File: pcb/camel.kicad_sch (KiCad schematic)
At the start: 49 parts, among them J1 Conn_01x04, J2 Conn_01x04, Q1 MMBT4403, Q2 MMBT4403, U1 HX711, U2 HX711, U3 MCP1700T-3302E/TT, Y1 11.0592MHz, Y2 11.0592MHz

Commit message: first pass
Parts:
- removed C13: 10u, Capacitor_SMD:C_0603_1608Metric, symbol Device:C_Small
- removed FPC1: FPC-05F-12PH15, EasyEDA2KiCAD:FPC-SMD_12P-P0.50_XUNPU_FPC-05F-12PH15, symbol EasyEDA2KiCAD:FPC-05F-12PH15
- removed JP1, JP4, JP6: SolderJumper_2_Bridged, Jumper:SolderJumper-2_P1.3mm_Bridged_RoundedPad1.0x1.5mm, symbol Jumper:SolderJumper_2_Bridged
- removed JP2, JP3: SolderJumper_3_Bridged12, Jumper:SolderJumper-3_P1.3mm_Bridged12_RoundedPad1.0x1.5mm, symbol Jumper:SolderJumper_3_Bridged12
- removed JP5, JP7: SolderJumper_2_Open, Jumper:SolderJumper-2_P1.3mm_Open_RoundedPad1.0x1.5mm, symbol Jumper:SolderJumper_2_Open
- removed R10, R9: 20K, Resistor_SMD:R_0402_1005Metric, symbol Device:R_Small
- removed Y1, Y2: 11.0592MHz, Crystal:Crystal_SMD_5032-4Pin_5.0x3.2mm, symbol Device:Crystal_GND24_Small
- added C15, C7, C8: 100n, Capacitor_SMD:C_0402_1005Metric, symbol Device:C_Small
- added C3: 10n, Capacitor_SMD:C_0402_1005Metric, symbol Device:C_Small
- added C4: 1u, Capacitor_SMD:C_0402_1005Metric, symbol Device:C_Small
- added D1: RED, LED_SMD:LED_0603_1608Metric, symbol Device:LED_Small
- added D10, D11, D2, D3, D4, D5, D6, D7, D8, D9: RCLAMP0521P-N, camel:X1-DFN1006-2_L1.0-W0.6-BI, symbol camel:RCLAMP0521P-N
- added H3, H4: MountingHole, MountingHole:MountingHole_3.5mm, symbol Mechanical:MountingHole
- added J2: TC2030-NL, Connector:Tag-Connect_TC2030-IDC-NL_2x03_P1.27mm_Vertical, symbol Connector:Conn_ARM_SWD_TagConnect_TC2030-NL
- added J3: USART, Connector_JST:JST_PH_S4B-PH-K_1x04_P2.00mm_Horizontal, symbol Connector_Generic:Conn_01x04
- added J5: I2C STEMMA, Connector_JST:JST_PH_S4B-PH-K_1x04_P2.00mm_Horizontal, symbol Connector_Generic:Conn_01x04
- added L1: 39n, Inductor_SMD:L_1008_2520Metric, symbol Device:L_Small
- added R4: 2K2, Resistor_SMD:R_0402_1005Metric, symbol Device:R_Small
- added R8: 10K, Resistor_SMD:R_0402_1005Metric, symbol Device:R_Small
- added U3: STM32L010F4P6, Package_SO:TSSOP-20_4.4x6.5mm_P0.65mm, symbol MCU_ST_STM32L0:STM32L010F4Px
- C10: value 10u -> 100n; footprint Capacitor_SMD:C_0603_1608Metric -> Capacitor_SMD:C_0402_1005Metric; Comment 25V 10uF X5R ±20% 0603 Multilayer Ceramic Capacitors MLCC -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 -> 16V 100nF X7R ±10% 0402 Multilayer Ceramic Capacitors MLCC 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; LCSC C96446 -> C1525; MFRN CL10A106MA8NRNC -> CL05B104KO5NNNC; PKG 0603 -> 0402
- C9: renamed from C14; value 0.1u -> 100n
- J1: footprint dualScaleBoard_hx711:Pad_1x04_P2.54mm -> camel:Pad_1x04_P2.54mm
- J4: renamed from J2; footprint dualScaleBoard_hx711:Pad_1x04_P2.54mm -> camel:Pad_1x04_P2.54mm
- Q1, Q2: symbol PCM_Transistor_BJT_AKL:MMBT4403 -> Transistor_BJT:MMBT3906
- U2: renamed from U1; footprint EasyEDA2KiCAD:SOP-16_L10.0-W3.9-P1.27-LS6.0-BL -> Package_SO:SOP-16_3.9x9.9mm_P1.27mm
- U4: renamed from U2; footprint EasyEDA2KiCAD:SOP-16_L10.0-W3.9-P1.27-LS6.0-BL -> Package_SO:SOP-16_3.9x9.9mm_P1.27mm
- renumbered C15 to C1, C1 to C11, C3 to C12, C5 to C13, C7 to C14, C2 to C17, C4 to C18, C6 to C19, C9 to C2, C8 to C20, C11 to C5, C12 to C6, H101 to H1, H102 to H2, L1 to L2, L2 to L3, R5 to R1, R8 to R10, R3 to R11, R4 to R12, R6 to R2, R1 to R3, R2 to R5, R7 to R9, U3 to U1
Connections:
- net VO is gone; now on net +3V3: U1.2 (VO)
- net DOUT1: now also U3.13 (PA7)
- net DOUT2: now also U3.12 (PA6)
- net GND: now also U2.14 (XI), U2.15 (RATE), U4.14 (XI), U4.15 (RATE), C15.1, C3.2, C4.2, C7.2, C8.2, D1.1 (K), D10.1, D11.1, D2.2, D3.2, D4.2, D5.2, D6.2, D7.2, D8.2, D9.2, J2.5 (GND), J3.4 (Pin_4), J5.4 (Pin_4), R8.2, U3.15 (VSS)
- net SCK1: now also U3.14 (PB1)
- net SCK2: now also U3.11 (PA5)
- net VCC renamed +5VA
- net +5VA: now also C3.1, C4.1, L1.1; no longer C10.1, C5.1, U1.3 (VI)
- net VDD renamed +3V3
- net +3V3: now also C10.1, C7.1, C8.1, D2.1, D6.1, J2.1 (VCC), J3.1 (Pin_1), U3.16 (VDD), U3.5 (VDDA)
- new net: D1.2 (A), R4.2
- new net +5V: C5.1, D9.1, J5.3 (Pin_3), L1.2, U1.3 (VI)
- new net BOOT0: R8.1, U3.1 (PB9)
- new net I2C_SCL: D10.2, J5.1 (Pin_1), U3.17 (PA9)
- new net I2C_SDA: D11.2, J5.2 (Pin_2), U3.18 (PA10)
- new net LED1: R4.1, U3.2 (PC14)
- new net NRST: C15.2, D5.1, J2.3 (~{RESET}), U3.4 (NRST)
- new net SWCLK: D4.1, J2.4 (SWCLK), U3.20 (PA14)
- new net SWDIO: D3.1, J2.2 (SWDIO), U3.19 (PA13)
- new net USART_RX: D7.1, J3.2 (Pin_2), U3.9 (PA3)
- new net USART_TX: D8.1, J3.3 (Pin_3), U3.8 (PA2)
- no-connect marks 0 -> 7
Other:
- note added: "Bridge Load Cell 1 (L)"
- note added: "Bridge Load Cell 2 (R)"
- note added: "Debugging/ Development"
- note added: "I2C lines can be pull up to 5V or 3V3 but supply must be 5V"
- note added: "Load Cell ADC 1 (L)"
- note added: "Load Cell ADC 2 (R)"
- note added: "MCU"
- note added: "Main I2C interface/Power Input"
- note added: "Serial Wire Debug (Programming)"
- note added: "Total power ~ 8mA"
- note removed: "10SPS"
- note removed: "3V3"
- note removed: "5V"
- note removed: "80SPS"
- note removed: "Int 3V3 VDD"
- note removed: "Internal Oscillator"
- note removed: "Optional Crystal"
- note removed: "Rate"
- note removed: "Shared CLK"
- note removed: "Shared VCC/VDD"
- company: (none) -> MetaQuantus
- title: (none) -> Camel I2C Dual Weigh Scales Board
- moved on the sheet: C1, C14, C2, C20, C5, C6, C9, FID1, FID2, FID3, H1, H2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

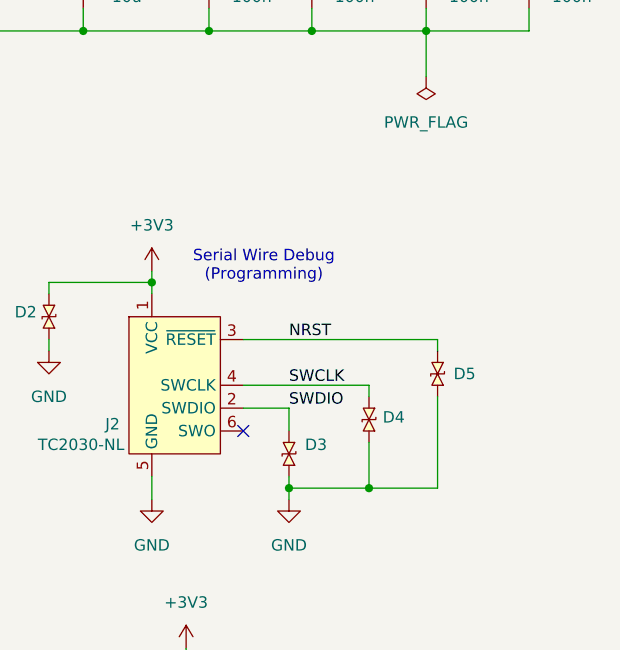
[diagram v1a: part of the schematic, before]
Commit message: added extra SWD connector in addition to TagConnect
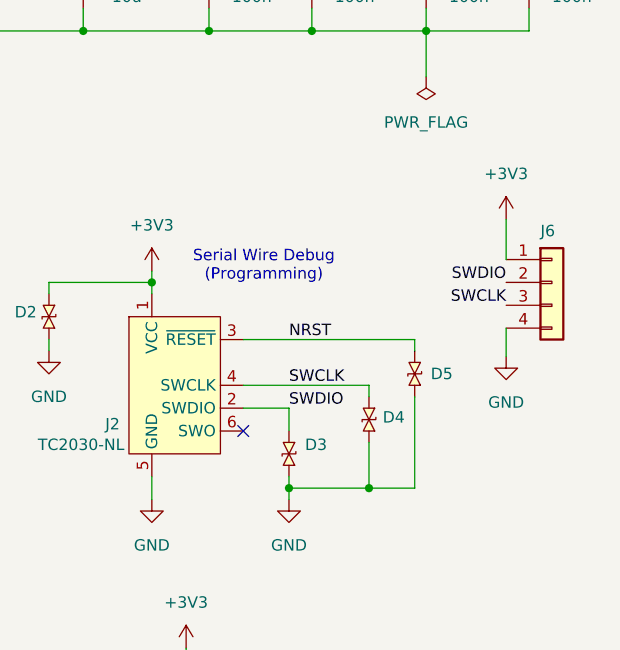
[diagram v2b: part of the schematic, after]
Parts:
- added J6: Conn_01x04, camel:Pad_1x04_P2.54mm, symbol Connector_Generic:Conn_01x04
- H1, H2, H3, H4: footprint MountingHole:MountingHole_3.5mm -> MountingHole:MountingHole_3.2mm_M3
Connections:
- net +3V3: now also J6.1 (Pin_1)
- net GND: now also J6.4 (Pin_4)
- net SWCLK: now also J6.3 (Pin_3)
- net SWDIO: now also J6.2 (Pin_2)
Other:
- moved on the sheet: D5

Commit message: replaced with hx712, updated schematics and pcb
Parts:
- removed C12, C18: 10u, Capacitor_SMD:C_0603_1608Metric, symbol Device:C_Small
- removed C17, C19, C20: 0.1u, Capacitor_SMD:C_0402_1005Metric, symbol Device:C_Small
- removed J4: Conn_01x04, camel:Pad_1x04_P2.54mm, symbol Connector_Generic:Conn_01x04
- removed L2, L3: 3.3u, Inductor_SMD:L_0603_1608Metric, symbol Device:L_Small
- removed Q1, Q2: MMBT4403, Package_TO_SOT_SMD:SOT-23, symbol Transistor_BJT:MMBT3906
- removed R11, R12, R5: 100R, Resistor_SMD:R_0402_1005Metric, symbol Device:R_Small
- removed U2, U4: HX711, Package_SO:SOP-16_3.9x9.9mm_P1.27mm, symbol Analog_ADC:HX711
- added C15: 0.1u, Capacitor_SMD:C_0402_1005Metric, symbol Device:C_Small
- added J5: Conn_01x04, camel:Pad_1x04_P2.54mm, symbol Connector_Generic:Conn_01x04
- added R4: 200R, Resistor_SMD:R_0402_1005Metric, symbol Device:R_Small
- added R7, R8: 100R, Resistor_SMD:R_0402_1005Metric, symbol Device:R_Small
- added U2, U4: HX712, Package_SO:SOIC-14_3.9x8.7mm_P1.27mm, symbol camel:HX712
- R1: value 20K -> 100R; Comment 60mW Thin Film Resistor ±0.1% ±10ppm/℃ 20kΩ 0402 Chip Resis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 -> 60mW Thin Film Resistor ±0.1% ±10ppm/℃ 100Ω 0402 Chip Resis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; LCSC C351700 -> C328416; MFRN PTFR0402B20K0N9 -> PTFR0402B100RN9
- R10: value 8K2 -> 200R; Comment 62.5mW ±50ppm/℃ ±0.1% 8.2kΩ 0402 Chip Resistor - Surface Mo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 -> 100mW Thick Film Resistors ±100ppm/℃ ±1% 200Ω 0402 Chip Res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; LCSC C517526 -> C328416; LCSCN (none) -> C413070; MANUFACTURER UNI-ROYAL(Uniroyal Elec) -> PANASONIC; MFRN TC0250B8201TCC -> ERJ2RKF2000X
- R2: value 8K2 -> 100R; Comment 62.5mW ±50ppm/℃ ±0.1% 8.2kΩ 0402 Chip Resistor - Surface Mo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 -> 60mW Thin Film Resistor ±0.1% ±10ppm/℃ 100Ω 0402 Chip Resis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; LCSC C517526 -> C328416; MANUFACTURER UNI-ROYAL(Uniroyal Elec) -> RESI; MFRN TC0250B8201TCC -> PTFR0402B100RN9
- R3: value 100R -> 200R; Comment 60mW Thin Film Resistor ±0.1% ±10ppm/℃ 100Ω 0402 Chip Resis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 -> 100mW Thick Film Resistors ±100ppm/℃ ±1% 200Ω 0402 Chip Res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; LCSCN (none) -> C413070; MANUFACTURER RESI -> PANASONIC; MFRN PTFR0402B100RN9 -> ERJ2RKF2000X
- R9: value 20K -> 200R; Comment 60mW Thin Film Resistor ±0.1% ±10ppm/℃ 20kΩ 0402 Chip Resis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 -> 100mW Thick Film Resistors ±100ppm/℃ ±1% 200Ω 0402 Chip Res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; LCSC C351700 -> C328416; LCSCN (none) -> C413070; MANUFACTURER RESI -> PANASONIC; MFRN PTFR0402B20K0N9 -> ERJ2RKF2000X
- renumbered C13 to C12, C15 to C13, D2 to D1, D9 to D11, D5 to D2, D4 to D3, D3 to D4, D1 to D5, D11 to D9, J6 to J2, J2 to J3, J3 to J4, J5 to J6, R4 to R5, R8 to R6
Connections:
- net +3V3: now also U2.13 (DVDD), U4.13 (DVDD)
- net +5VA: now also U2.1 (AVDD), U2.14 (BAT), U4.1 (AVDD), U4.14 (BAT)
- net DOUT1: now also U2.10 (DOUT)
- net DOUT2: now also U4.10 (DOUT)
- net GND: now also R2.1, R8.1, U2.12 (XI), U2.4 (AGND), U2.8 (DGND), U4.12 (XI), U4.4 (AGND), U4.8 (DGND); no longer C11.2, C14.2, J1.2 (Pin_2), R10.2, R2.2
- net SCK1: now also U2.9 (PD_SCK)
- net SCK2: now also U4.9 (PD_SCK)
- net at C14.1: now also J5.1 (Pin_1), R7.1, U4.3 (REFP)
- net at R1.1: now also C11.1, J1.1 (Pin_1), U2.3 (REFP)
- net at R1.2: now also U2.2 (VOUT); no longer R2.1
- net at C12.2: now also R4.2, U2.7 (INP)
- net at C12.1, R3.2: now also U2.6 (INN)
- net at R3.1: now also J1.3 (Pin_3); no longer J1.4 (Pin_4)
- net at R9.1: now also J5.3 (Pin_3)
- net at R10.1: now also J5.4 (Pin_4); no longer R9.2
- new net: C14.2, J5.2 (Pin_2), R8.2, U4.5 (REFN)
- new net: C15.2, R10.2, U4.7 (INP)
- new net: C11.2, J1.2 (Pin_2), R2.2, U2.5 (REFN)
- new net: J1.4 (Pin_4), R4.1
- new net: R7.2, U4.2 (VOUT)
- new net: C15.1, R9.2, U4.6 (INN)
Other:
- note added: "A+(GRN)"
- note added: "A-(WHT)"
- note added: "E+(RED)"
- note added: "E-(BLK)"
- moved on the sheet: C11, C12, J1, R3

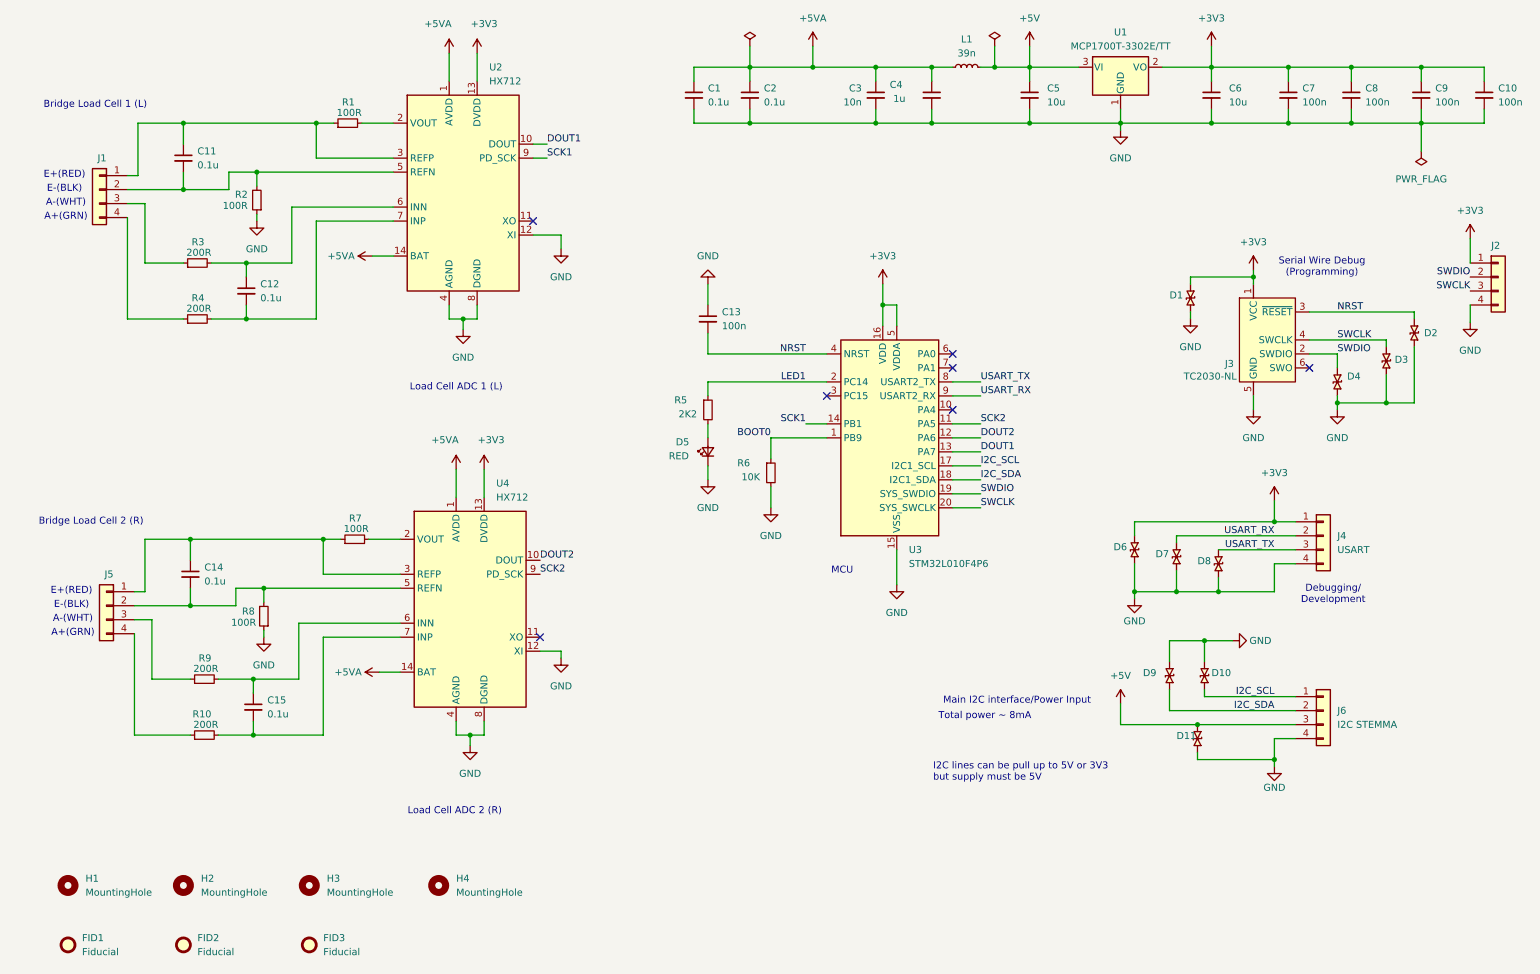
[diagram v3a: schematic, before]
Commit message: PCB updates, teardrops and trace cleanup
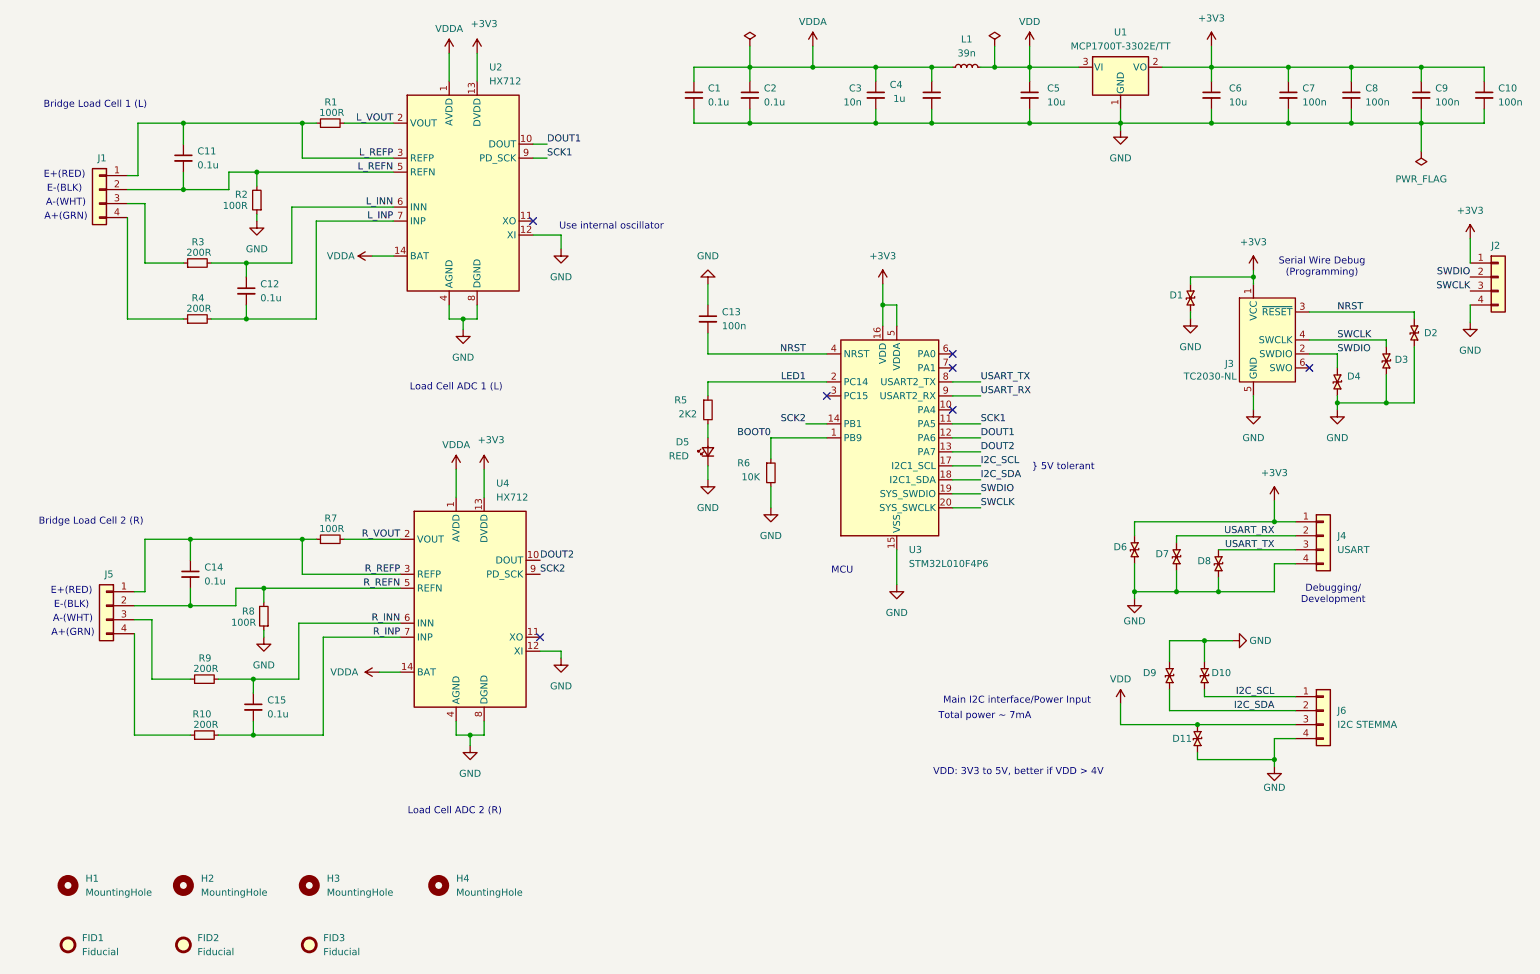
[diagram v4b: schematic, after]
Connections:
- net DOUT1: now also U3.12 (PA6); no longer U3.13 (PA7)
- net DOUT2: now also U3.13 (PA7); no longer U3.12 (PA6)
- net SCK1: now also U3.11 (PA5); no longer U3.14 (PB1)
- net SCK2: now also U3.14 (PB1); no longer U3.11 (PA5)
- net L_INN: now reaches C12.1, R3.2, U2.6 (INN)
- net L_INP: now reaches C12.2, R4.2, U2.7 (INP)
- net R_REFP: now reaches C14.1, J5.1 (Pin_1), R7.1, U4.3 (REFP)
- net R_REFN: now reaches C14.2, J5.2 (Pin_2), R8.2, U4.5 (REFN)
- net R_INP: now reaches C15.2, R10.2, U4.7 (INP)
- net L_REFP: now reaches C11.1, J1.1 (Pin_1), R1.1, U2.3 (REFP)
- net L_REFN: now reaches C11.2, J1.2 (Pin_2), R2.2, U2.5 (REFN)
- net L_VOUT: now reaches R1.2, U2.2 (VOUT)
- net R_VOUT: now reaches R7.2, U4.2 (VOUT)
- net R_INN: now reaches C15.1, R9.2, U4.6 (INN)
- net +5V renamed VDD
- net +5VA renamed VDDA
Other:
- note added: "Total power ~ 7mA"
- note added: "Use internal oscillator"
- note added: "VDD: 3V3 to 5V, better if VDD > 4V"
- note added: "} 5V tolerant"
- note removed: "I2C lines can be pull up to 5V or 3V3 but supply must be 5V"
- note removed: "Total power ~ 8mA"
- moved on the sheet: R1, R7

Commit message: PCB refactoring, BOM updates, firmware added EEPROM storage of configuration
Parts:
- C1, C11, C12, C14, C15, C2: value 0.1u -> 100n
- D5: Comment Colorless transparence 624nm~624nm -40℃~+85℃ Red 60° 60mW 1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 -> -40℃~+85℃ Red 0603 LED Indication - Discrete ROHS; LCSC C648676 -> C2286; MANUFACTURER Everlight Elec -> Hubei KENTO Elec; MFRN 11-21SURC/S530-A6/TR8 -> KT-0603R
- R10, R3, R4, R9: LCSC C328416 -> C413070; LCSCN C413070 -> (none)
- U2, U4: Comment (none) -> 24Bit 2.6V~5.5V SOP-14 Analog to Digital Converters (ADC) R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; LCSC (none) -> C118237; MANUFACTURER (none) -> Avia Semicon (Xiamen); MFRN (none) -> HX712; PKG (none) -> SOP-14
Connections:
- net +3V3: now also L1.2, U2.14 (BAT), U4.14 (BAT)
- net VDD: no longer L1.2
- net VDDA: no longer U2.14 (BAT), U4.14 (BAT)
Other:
- moved on the sheet: C3, C4, L1
